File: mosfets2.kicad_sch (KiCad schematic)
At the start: 38 parts, among them Q1 IXFK300N20X3, Q2 IXFK300N20X3, Q3 IXFK300N20X3, Q4 IXFK300N20X3, Q5 IXFK300N20X3, Q6 IXFK300N20X3, U1 ACS781xLRTR-150B, U2 ACS781xLRTR-150B, U3 ACS781xLRTR-150B

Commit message: - some layout work
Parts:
- removed C29: 100n, Capacitor_SMD:C_0805_2012Metric, symbol Device:C
- removed C30: 1u, Capacitor_SMD:C_0805_2012Metric, symbol Device:C
- removed C31: 4n7, Capacitor_SMD:C_0805_2012Metric, symbol Device:C
- removed R26: 1k, Resistor_SMD:R_0805_2012Metric, symbol Device:R
- removed U3: ACS781xLRTR-150B, Sensor_Current:Allegro_PSOF-7_4.8x6.4mm_P1.60mm, symbol Sensor_Current:ACS781xLRTR-150B
- C20, C21, C22, C23, C24, C25: footprint Capacitor_SMD:C_2220_5650Metric -> Capacitor_SMD:C_2220_5750Metric
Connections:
- no-connect marks 6 -> 4

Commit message: - layout almost finished
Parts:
- removed C12, C26: 100n, Capacitor_SMD:C_0805_2012Metric, symbol Device:C
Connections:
- net U renamed U2
- net U_GH renamed U2_GH
- net U_GL renamed U2_GL
- net U_I renamed U2_I
- net U_VP renamed U2_VP
- net V renamed V2
- net V_GH renamed V2_GH
- net V_GL renamed V2_GL
- net V_I renamed V2_I
- net V_VP renamed V2_VP
- net W_GH renamed W2_GH
- net W_GL renamed W2_GL
- net W_VP renamed W2

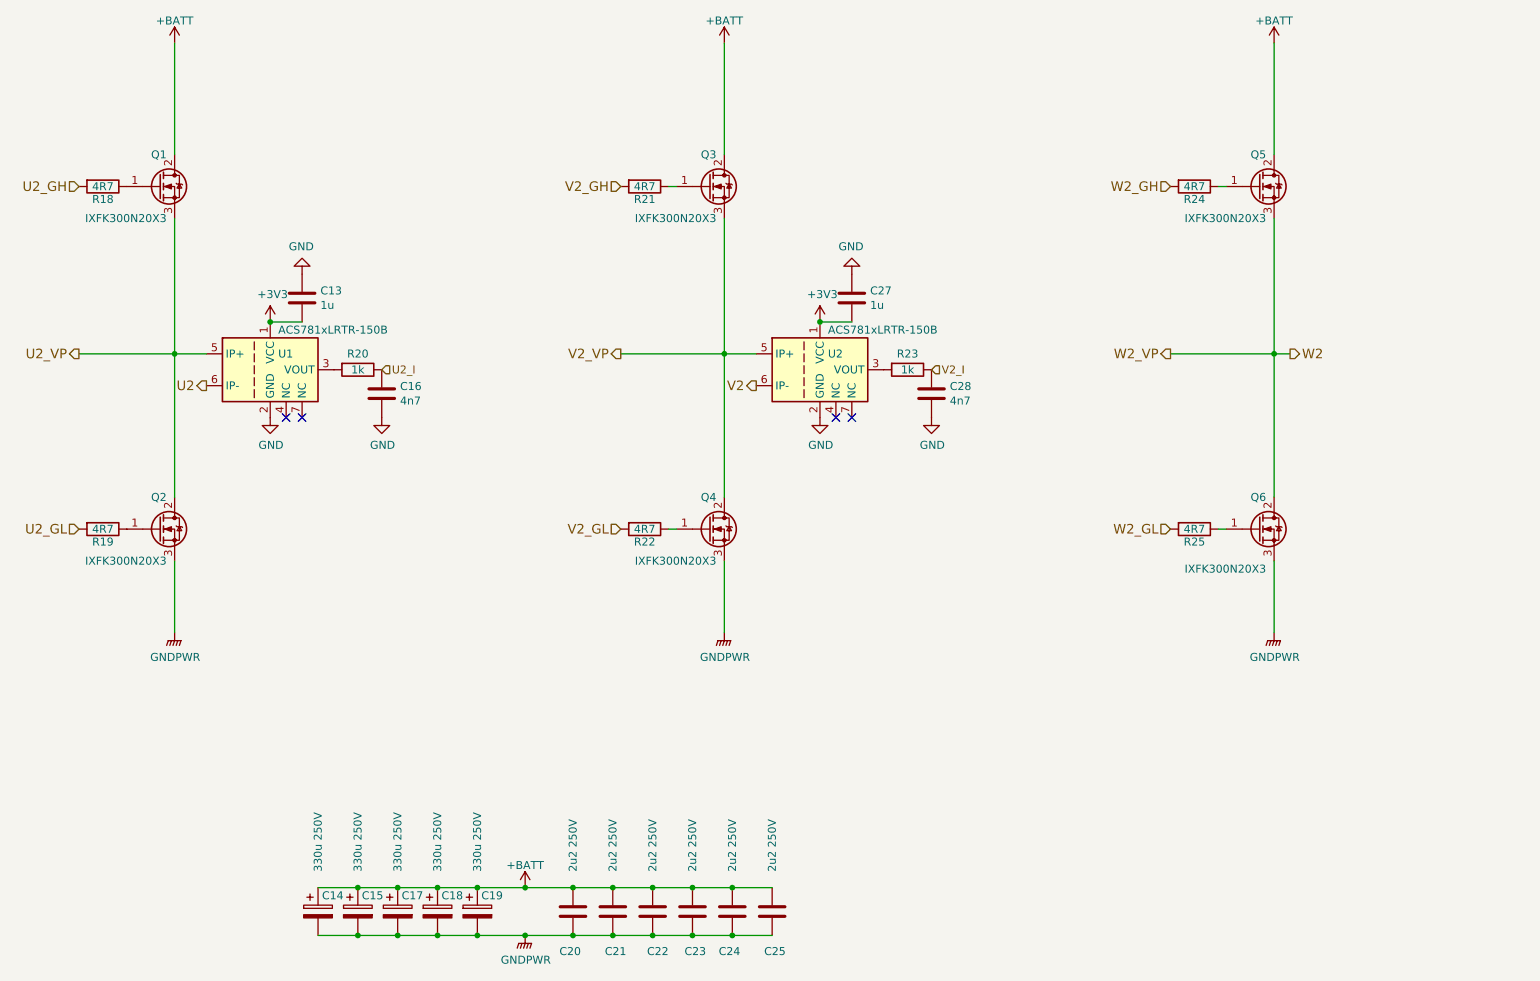
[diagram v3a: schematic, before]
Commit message: - fixed missing 3V3 trace on USB isolator
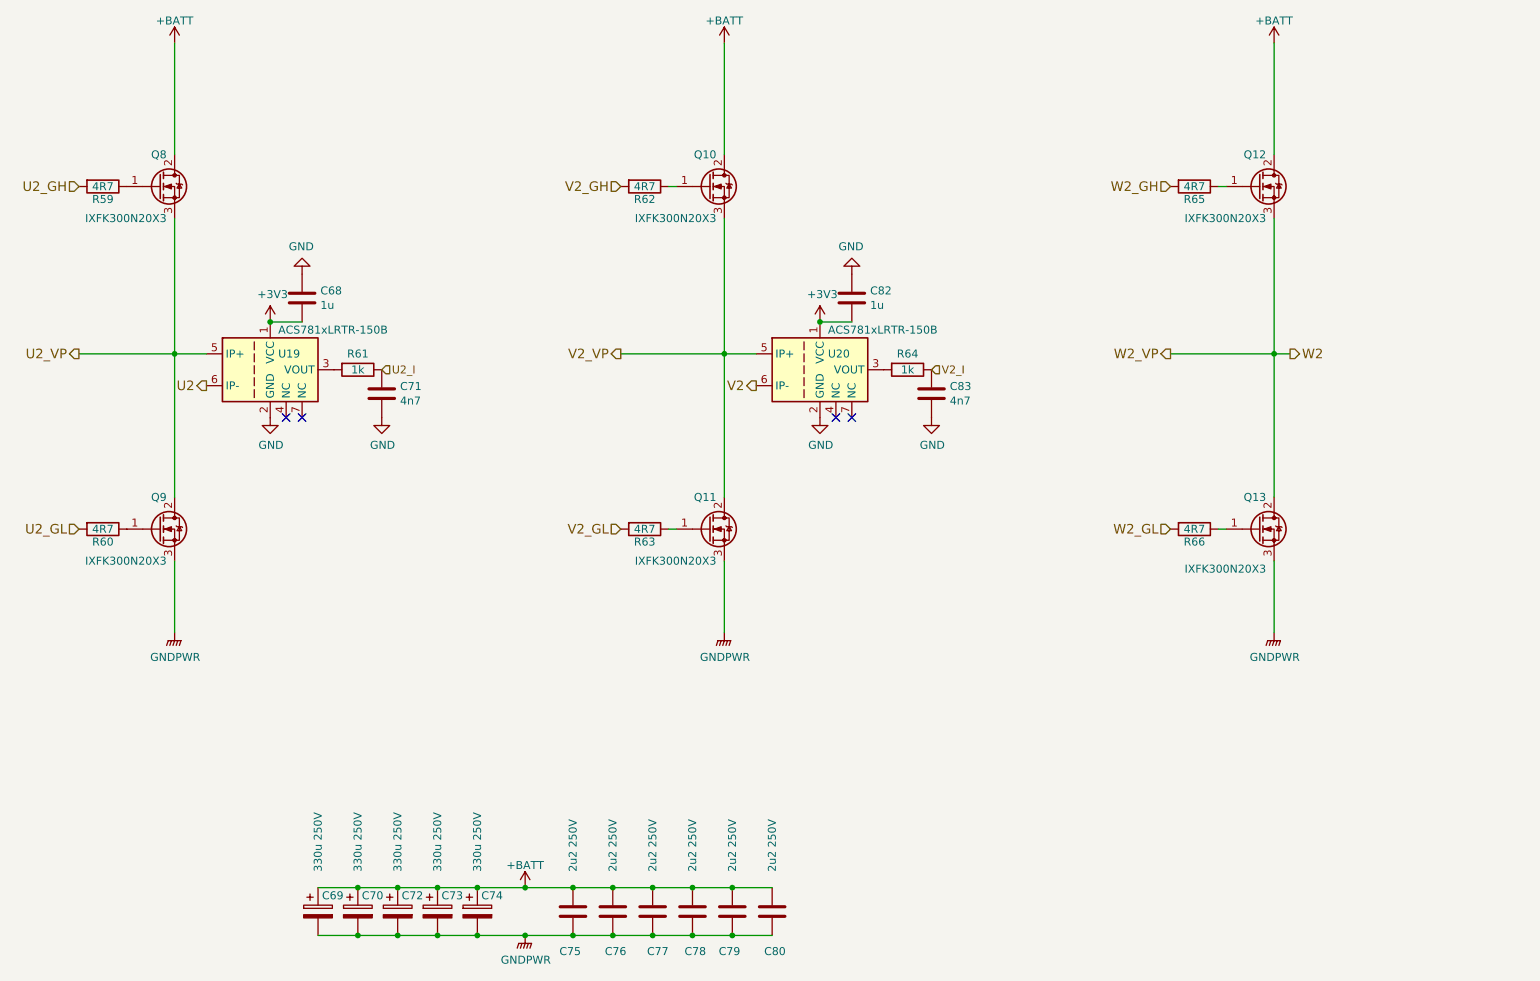
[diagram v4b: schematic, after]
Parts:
- renumbered C13 to C68, C14 to C69, C15 to C70, C16 to C71, C17 to C72, C18 to C73, C19 to C74, C20 to C75, C21 to C76, C22 to C77, C23 to C78, C24 to C79, C25 to C80, C27 to C82, C28 to C83, Q3 to Q10, Q4 to Q11, Q5 to Q12, Q6 to Q13, Q1 to Q8, Q2 to Q9, R18 to R59, R19 to R60, R20 to R61, R21 to R62, R22 to R63, R23 to R64, R24 to R65, R25 to R66, U1 to U19, U2 to U20
